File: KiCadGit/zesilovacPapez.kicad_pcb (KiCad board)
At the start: 2 copper layers, 141.2 x 141.2 mm, 81 parts, among them P1 VDD, P10 BNC, P11 VDD, P12 GND, P13 BNC, P2 INPUT, P3 GND, P4 VDD, P5 GND, P6 BNC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

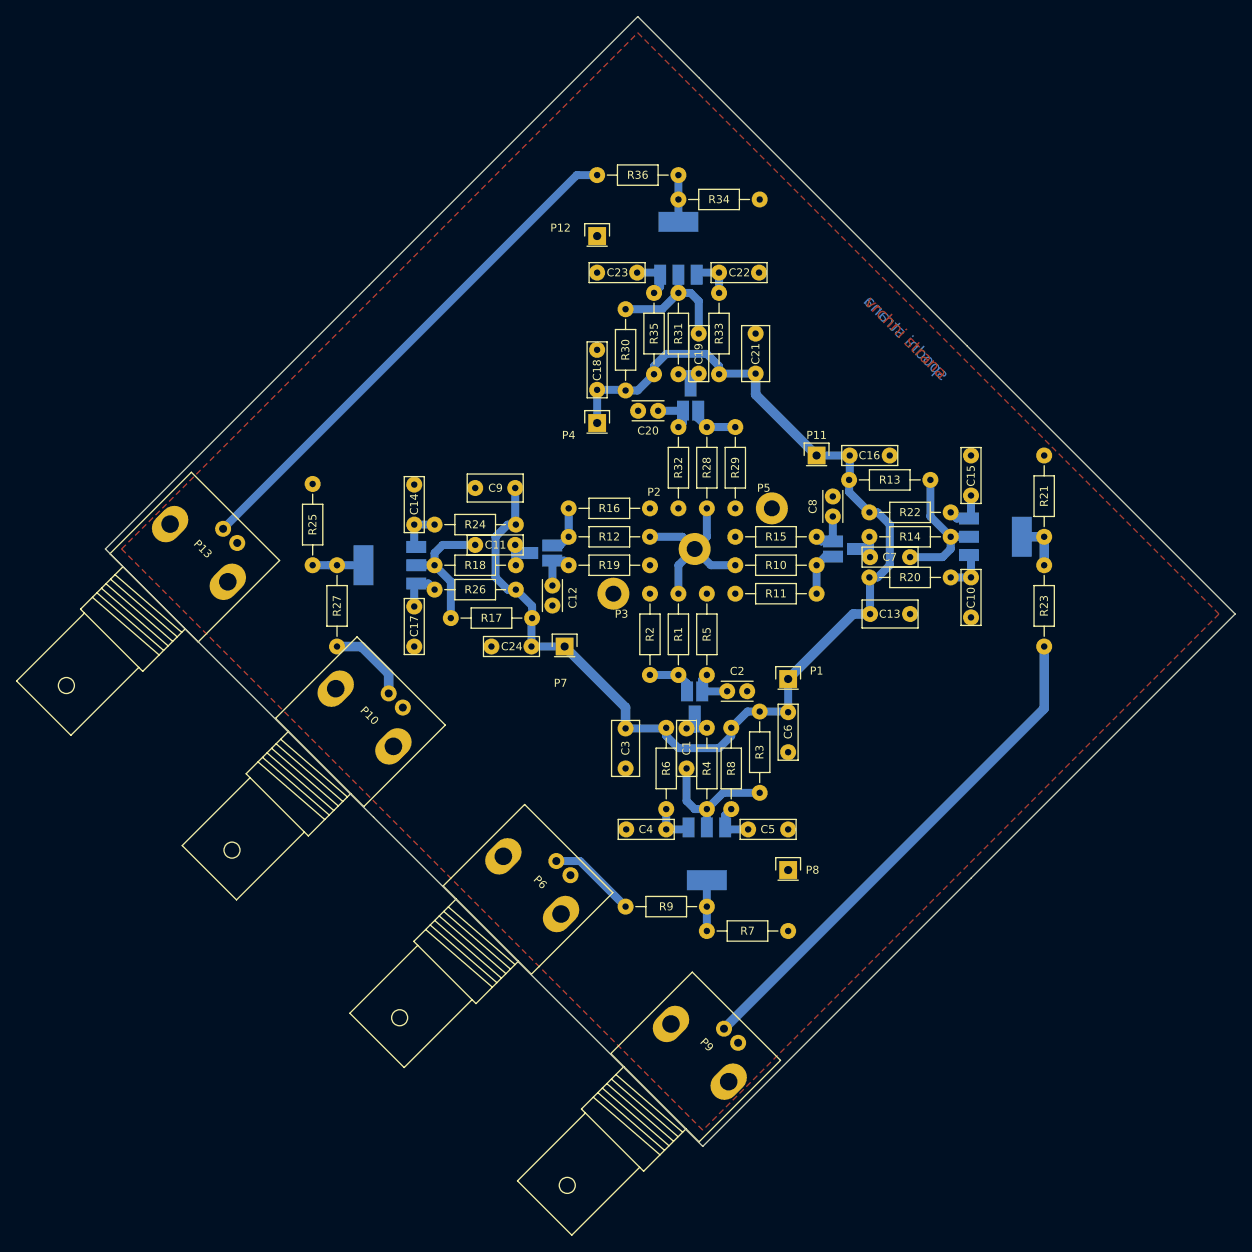
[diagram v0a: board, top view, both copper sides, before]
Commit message: Zesilovac Papez: - uprava potisku BNC pro vyrobu v Cine nebo Pragoboardu - vygenerovani gerber dat
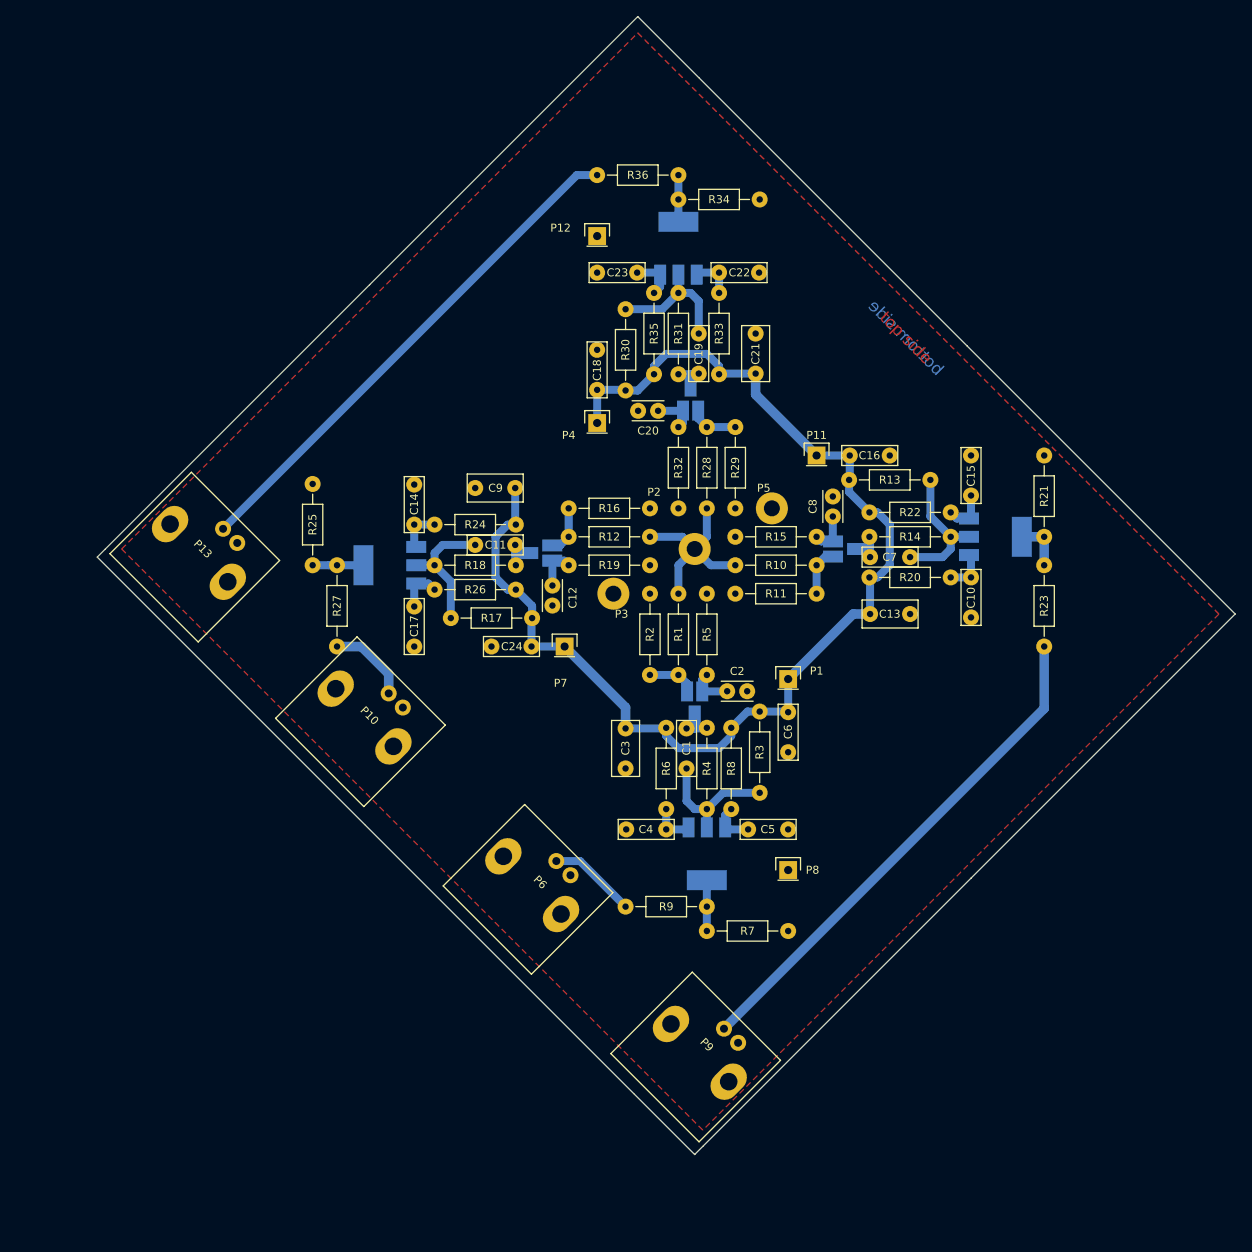
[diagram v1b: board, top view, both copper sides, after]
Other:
- board size 141.2 x 141.2 mm -> 142.2 x 142.2 mm
- board text added: "bottom side"
- board text added: "top side"
- board text removed: "spodni strana"
- board text removed: "vrchni strana"
